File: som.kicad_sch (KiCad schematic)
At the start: 24 parts, among them U201 74LVC2G17GV

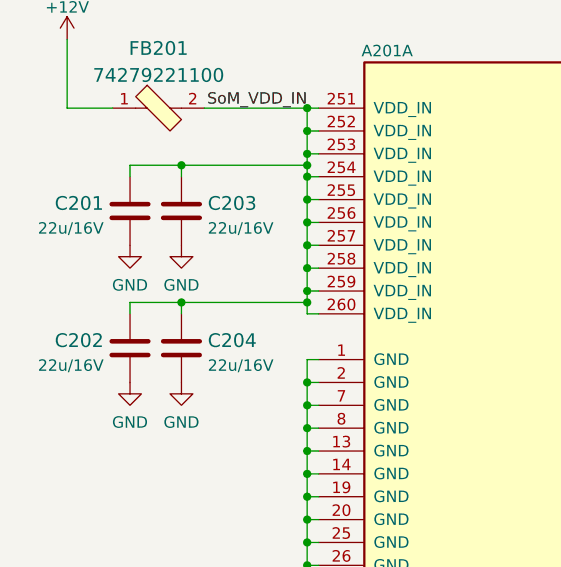
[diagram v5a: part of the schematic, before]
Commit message: Replace SoM VDD_IN caps with 25V rated ones
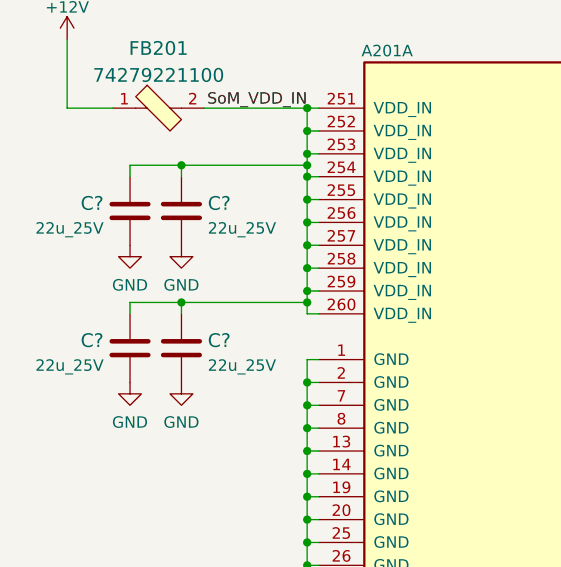
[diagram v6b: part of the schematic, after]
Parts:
- removed C201, C202, C203, C204: C_22u_0805_16V, antmicro-footprints:0805-cap, symbol antmicroCapacitorsmisc:C_22u_0805_16V
- added C? (x4): C_22u_0805_25V, antmicro-footprints:0805-cap, symbol antmicroCapacitorsmisc:C_22u_0805_25V
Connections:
- net GND: now also C?.2, C?.2, C?.2, C?.2
- net SoM_VDD_IN: now also C?.1, C?.1, C?.1, C?.1
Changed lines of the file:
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@@
-    (pin "2")
-  )
-  (symbol (lib_id "antmicroCapacitorsmisc:C_22u_0805_16V") (at 30.48 97.79 0) (unit 1)
-    (in_bom yes) (on_board yes) (fields_autoplaced)
-    (property "Reference" "C203" (id 0) (at 33.401 96.9554 0)
-      (effects (font (size 1.524 1.524)) (justify left))
-    )
-    (property "Value" "C_22u_0805_16V" (id 1) (at 30.48 101.6 0)
-      (effects (font (size 1.524 1.524)) hide)
-    )
-    (property "Footprint" "antmicro-footprints:0805-cap" (id 2) (at 35.56 92.71 0)
-      (effects (font (size 1.524 1.524)) (justify left) hide)
-    )
-    (property "Datasheet" "" (id 3) (at 30.48 97.79 0)
-      (effects (font (size 1.27 1.27)) hide)
-    )
-    (property "Manufacturer" "Murata" (id 4) (at 35.56 87.63 0)
-      (effects (font (size 1.524 1.524)) (justify left) hide)
-    )
-    (property "MPN" "GRT21BR61C226ME13L" (id 5) (at 35.56 90.17 0)
-      (effects (font (size 1.524 1.524)) (justify left) hide)
-    )
-    (property "Val" "22u/16V" (id 6) (at 33.401 99.7205 0)
-      (effects (font (size 1.27 1.27)) (justify left))
-    )
-    (pin "1")
     (pin "2")
   )
@@
     (pin "1")
   )
-  (symbol (lib_id "antmicroCapacitorsmisc:C_22u_0805_16V") (at 24.765 113.03 0) (unit 1)
-    (in_bom yes) (on_board yes) (fields_autoplaced)
-    (property "Reference" "C202" (id 0) (at 21.844 112.1954 0)
-      (effects (font (size 1.524 1.524)) (justify right))
-    )
-    (property "Value" "C_22u_0805_16V" (id 1) (at 24.765 116.84 0)
-      (effects (font (size 1.524 1.524)) hide)
-    )
-    (property "Footprint" "antmicro-footprints:0805-cap" (id 2) (at 29.845 107.95 0)
-      (effects (font (size 1.524 1.524)) (justify left) hide)
-    )
-    (property "Datasheet" "" (id 3) (at 24.765 113.03 0)
-      (effects (font (size 1.27 1.27)) hide)
-    )
-    (property "Manufacturer" "Murata" (id 4) (at 29.845 102.87 0)
-      (effects (font (size 1.524 1.524)) (justify left) hide)
-    )
-    (property "MPN" "GRT21BR61C226ME13L" (id 5) (at 29.845 105.41 0)
-      (effects (font (size 1.524 1.524)) (justify left) hide)
-    )
-    (property "Val" "22u/16V" (id 6) (at 21.844 114.9605 0)
-      (effects (font (size 1.27 1.27)) (justify right))
-    )
-    (pin "1")
-    (pin "2")
-  )
   (symbol (lib_id "antmicroResistors0402:R_0R_0402") (at 196.85 35.56 0) (unit 1)
     (in_bom yes) (on_board yes)
@@
     (pin "2")
   )
-  (symbol (lib_id "antmicroCapacitorsmisc:C_22u_0805_16V") (at 30.48 113.03 0) (unit 1)
-    (in_bom yes) (on_board yes) (fields_autoplaced)
-    (property "Reference" "C204" (id 0) (at 33.401 112.1954 0)
-      (effects (font (size 1.524 1.524)) (justify left))
-    )
-    (property "Value" "C_22u_0805_16V" (id 1) (at 30.48 116.84 0)
-      (effects (font (size 1.524 1.524)) hide)
-    )
-    (property "Footprint" "antmicro-footprints:0805-cap" (id 2) (at 35.56 107.95 0)
-      (effects (font (size 1.524 1.524)) (justify left) hide)
-    )
-    (property "Datasheet" "" (id 3) (at 30.48 113.03 0)
-      (effects (font (size 1.27 1.27)) hide)
-    )
-    (property "Manufacturer" "Murata" (id 4) (at 35.56 102.87 0)
-      (effects (font (size 1.524 1.524)) (justify left) hide)
-    )
-    (property "MPN" "GRT21BR61C226ME13L" (id 5) (at 35.56 105.41 0)
-      (effects (font (size 1.524 1.524)) (justify left) hide)
-    )
-    (property "Val" "22u/16V" (id 6) (at 33.401 114.9605 0)
-      (effects (font (size 1.27 1.27)) (justify left))
-    )
-    (pin "1")
-    (pin "2")
-  )
-  (symbol (lib_id "antmicroCapacitorsmisc:C_22u_0805_16V") (at 24.765 97.79 0) (unit 1)
-    (in_bom yes) (on_board yes) (fields_autoplaced)
-    (property "Reference" "C201" (id 0) (at 21.844 96.9554 0)
-      (effects (font (size 1.524 1.524)) (justify right))
-    )
-    (property "Value" "C_22u_0805_16V" (id 1) (at 24.765 101.6 0)
-      (effects (font (size 1.524 1.524)) hide)
-    )
-    (property "Footprint" "antmicro-footprints:0805-cap" (id 2) (at 29.845 92.71 0)
-      (effects (font (size 1.524 1.524)) (justify left) hide)
-    )
-    (property "Datasheet" "" (id 3) (at 24.765 97.79 0)
-      (effects (font (size 1.27 1.27)) hide)
-    )
-    (property "Manufacturer" "Murata" (id 4) (at 29.845 87.63 0)
-      (effects (font (size 1.524 1.524)) (justify left) hide)
-    )
-    (property "MPN" "GRT21BR61C226ME13L" (id 5) (at 29.845 90.17 0)
-      (effects (font (size 1.524 1.524)) (justify left) hide)
-    )
-    (property "Val" "22u/16V" (id 6) (at 21.844 99.7205 0)
-      (effects (font (size 1.27 1.27)) (justify right))
-    )
-    (pin "1")
-    (pin "2")
-  )
   (symbol (lib_id "antmicroResistors0402:R_0R_0402") (at 198.12 66.04 0) (mirror x) (unit 1)
     (in_bom yes) (on_board yes)
@@
     )
     (pin "1")
+  )
+  (symbol (lib_id "antmicroCapacitorsmisc:C_22u_0805_25V") (at 30.48 97.79 0) (unit 1)
+    (in_bom yes) (on_board yes) (fields_autoplaced)
+    (property "Reference" "C?" (id 0) (at 33.401 96.9554 0)
+      (effects (font (size 1.524 1.524)) (justify left))
+    )
+    (property "Value" "C_22u_0805_25V" (id 1) (at 30.48 101.6 0)
+      (effects (font (size 1.524 1.524)) hide)
+    )
+    (property "Footprint" "antmicro-footprints:0805-cap" (id 2) (at 35.56 92.71 0)
+      (effects (font (size 1.524 1.524)) (justify left) hide)
+    )
+    (property "Datasheet" "" (id 3) (at 30.48 97.79 0)
+      (effects (font (size 1.27 1.27)) hide)
+    )
+    (property "Manufacturer" "Samsung Electro-Mechanics" (id 4) (at 35.56 87.63 0)
+      (effects (font (size 1.524 1.524)) (justify left) hide)
+    )
+    (property "MPN" "CL21A226MAYNNNE" (id 5) (at 35.56 90.17 0)
+      (effects (font (size 1.524 1.524)) (justify left) hide)
+    )
+    (property "Val" "22u_25V" (id 6) (at 33.401 99.7205 0)
+      (effects (font (size 1.27 1.27)) (justify left))
+    )
+    (pin "1")
+    (pin "2")
   )
   (symbol (lib_id "power:GND") (at 97.79 212.09 0) (unit 1)
@@
     (pin "228")
   )
+  (symbol (lib_id "antmicroCapacitorsmisc:C_22u_0805_25V") (at 24.765 97.79 0) (unit 1)
+    (in_bom yes) (on_board yes) (fields_autoplaced)
+    (property "Reference" "C?" (id 0) (at 21.8441 96.9554 0)
+      (effects (font (size 1.524 1.524)) (justify right))
+    )
+    (property "Value" "C_22u_0805_25V" (id 1) (at 24.765 101.6 0)
+      (effects (font (size 1.524 1.524)) hide)
+    )
+    (property "Footprint" "antmicro-footprints:0805-cap" (id 2) (at 29.845 92.71 0)
+      (effects (font (size 1.524 1.524)) (justify left) hide)
+    )
+    (property "Datasheet" "" (id 3) (at 24.765 97.79 0)
+      (effects (font (size 1.27 1.27)) hide)
+    )
+    (property "Manufacturer" "Samsung Electro-Mechanics" (id 4) (at 29.845 87.63 0)
+      (effects (font (size 1.524 1.524)) (justify left) hide)
+    )
+    (property "MPN" "CL21A226MAYNNNE" (id 5) (at 29.845 90.17 0)
+      (effects (font (size 1.524 1.524)) (justify left) hide)
+    )
+    (property "Val" "22u_25V" (id 6) (at 21.8441 99.7205 0)
+      (effects (font (size 1.27 1.27)) (justify right))
+    )
+    (pin "1")
+    (pin "2")
+  )
   (symbol (lib_id "antmicroTestPoints:TP_SMD_0_75MM") (at 116.84 99.06 90) (unit 1)
     (in_bom yes) (on_board yes) (fields_autoplaced)
@@
     )
     (pin "1")
+  )
+  (symbol (lib_id "antmicroCapacitorsmisc:C_22u_0805_25V") (at 30.48 113.03 0) (unit 1)
+    (in_bom yes) (on_board yes) (fields_autoplaced)
+    (property "Reference" "C?" (id 0) (at 33.401 112.1954 0)
+      (effects (font (size 1.524 1.524)) (justify left))
+    )
+    (property "Value" "C_22u_0805_25V" (id 1) (at 30.48 116.84 0)
+      (effects (font (size 1.524 1.524)) hide)
+    )
+    (property "Footprint" "antmicro-footprints:0805-cap" (id 2) (at 35.56 107.95 0)
+      (effects (font (size 1.524 1.524)) (justify left) hide)
+    )
+    (property "Datasheet" "" (id 3) (at 30.48 113.03 0)
+      (effects (font (size 1.27 1.27)) hide)
+    )
+    (property "Manufacturer" "Samsung Electro-Mechanics" (id 4) (at 35.56 102.87 0)
+      (effects (font (size 1.524 1.524)) (justify left) hide)
+    )
+    (property "MPN" "CL21A226MAYNNNE" (id 5) (at 35.56 105.41 0)
+      (effects (font (size 1.524 1.524)) (justify left) hide)
+    )
+    (property "Val" "22u_25V" (id 6) (at 33.401 114.9605 0)
+      (effects (font (size 1.27 1.27)) (justify left))
+    )
+    (pin "1")
+    (pin "2")
   )
   (symbol (lib_id "antmicroPushbuttonSwitches:B3U-3000PM") (at 34.29 243.84 90) (mirror x) (unit 1)
@@
     (pin "1")
   )
+  (symbol (lib_id "antmicroCapacitorsmisc:C_22u_0805_25V") (at 24.765 113.03 0) (unit 1)
+    (in_bom yes) (on_board yes) (fields_autoplaced)
+    (property "Reference" "C?" (id 0) (at 21.8441 112.1954 0)
+      (effects (font (size 1.524 1.524)) (justify right))
+    )
+    (property "Value" "C_22u_0805_25V" (id 1) (at 24.765 116.84 0)
+      (effects (font (size 1.524 1.524)) hide)
+    )
+    (property "Footprint" "antmicro-footprints:0805-cap" (id 2) (at 29.845 107.95 0)
+      (effects (font (size 1.524 1.524)) (justify left) hide)
+    )
+    (property "Datasheet" "" (id 3) (at 24.765 113.03 0)
+      (effects (font (size 1.27 1.27)) hide)
+    )
+    (property "Manufacturer" "Samsung Electro-Mechanics" (id 4) (at 29.845 102.87 0)
+      (effects (font (size 1.524 1.524)) (justify left) hide)
+    )
+    (property "MPN" "CL21A226MAYNNNE" (id 5) (at 29.845 105.41 0)
+      (effects (font (size 1.524 1.524)) (justify left) hide)
+    )
+    (property "Val" "22u_25V" (id 6) (at 21.8441 114.9605 0)
+      (effects (font (size 1.27 1.27)) (justify right))
+    )
+    (pin "1")
+    (pin "2")
+  )
   (symbol (lib_id "power:GND") (at 30.48 101.6 0) (unit 1)

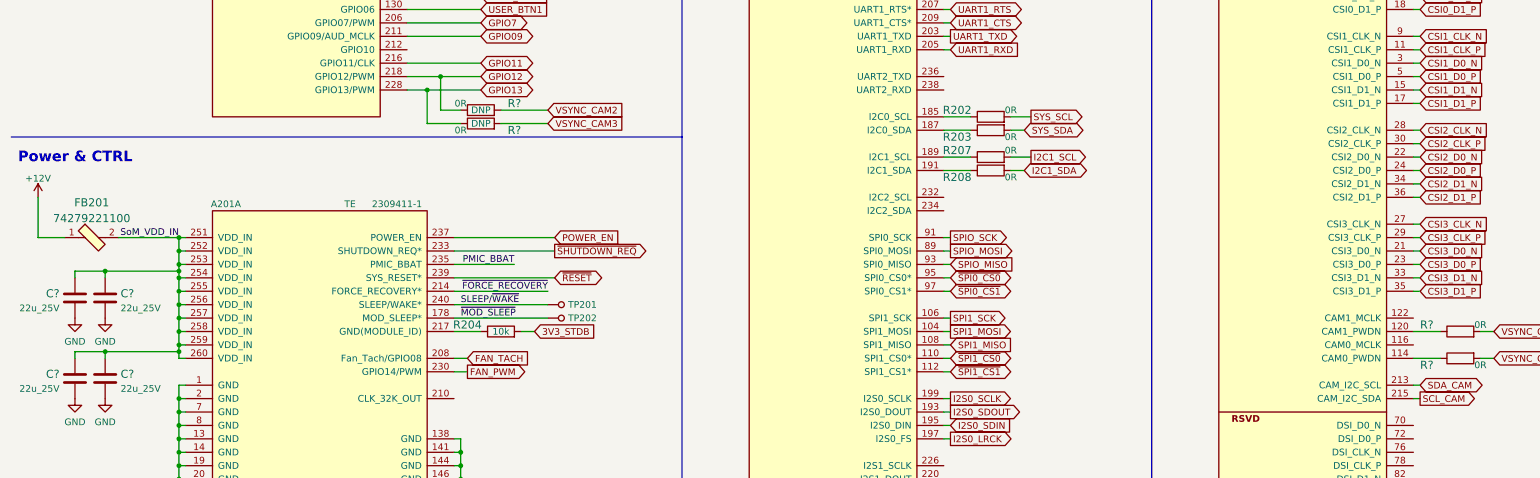
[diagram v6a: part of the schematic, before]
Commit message: Cleaned up the schematic, fixed library issues, annotated schematic
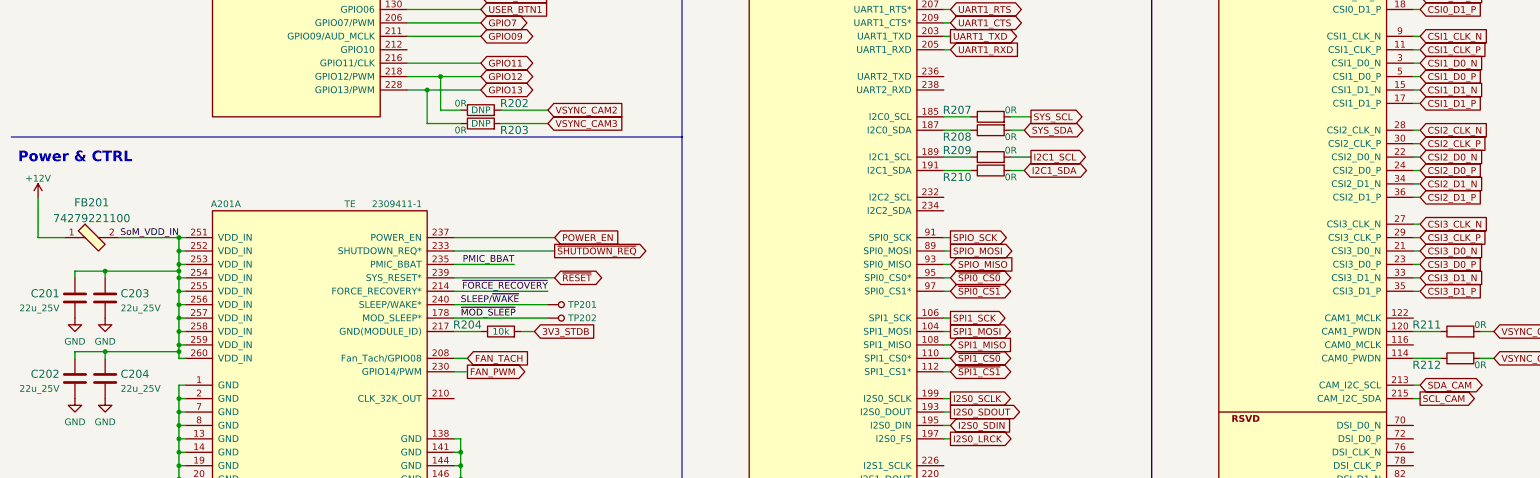
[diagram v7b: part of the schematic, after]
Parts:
- gave numbers to parts that had none: 8
- renumbered R202 to R207, R203 to R208, R207 to R209, R208 to R210
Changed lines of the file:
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@@
   (title_block
     (title "Jetson Orin NX Baseboard")
+    (date "2022-09-28")
+    (rev "0.1.0")
     (company "Antmicro Ltd")
     (comment 1 "www.antmicro.com")
@@
   (symbol (lib_id "antmicroResistors0402:R_0R_0402") (at 198.12 63.5 0) (unit 1)
     (in_bom yes) (on_board yes)
-    (property "Reference" "R202" (id 0) (at 191.77 62.23 0)
+    (property "Reference" "R207" (id 0) (at 191.77 62.23 0)
       (effects (font (size 1.524 1.524)))
     )
@@
   (symbol (lib_id "power:GND") (at 44.45 212.09 0) (unit 1)
     (in_bom yes) (on_board yes) (fields_autoplaced)
-    (property "Reference" "#PWR0206" (id 0) (at 44.45 218.44 0)
+    (property "Reference" "#PWR0207" (id 0) (at 44.45 218.44 0)
       (effects (font (size 1.27 1.27)) hide)
     )
@@
   (symbol (lib_id "antmicroResistors0402:R_0R_0402") (at 198.12 73.66 0) (mirror x) (unit 1)
     (in_bom yes) (on_board yes)
-    (property "Reference" "R208" (id 0) (at 191.77 74.93 0)
+    (property "Reference" "R210" (id 0) (at 191.77 74.93 0)
       (effects (font (size 1.524 1.524)))
     )
@@
   (symbol (lib_id "antmicroResistors0402:R_0R_0402") (at 198.12 71.12 0) (unit 1)
     (in_bom yes) (on_board yes)
-    (property "Reference" "R207" (id 0) (at 191.77 69.85 0)
+    (property "Reference" "R209" (id 0) (at 191.77 69.85 0)
       (effects (font (size 1.524 1.524)))
     )
@@
   (symbol (lib_id "power:GND") (at 64.77 250.19 0) (unit 1)
     (in_bom yes) (on_board yes) (fields_autoplaced)
-    (property "Reference" "#PWR0209" (id 0) (at 64.77 256.54 0)
+    (property "Reference" "#PWR0208" (id 0) (at 64.77 256.54 0)
       (effects (font (size 1.27 1.27)) hide)
     )
@@
   (symbol (lib_id "antmicroResistors0402:R_0R_0402") (at 101.6 64.77 0) (unit 1)
     (in_bom yes) (on_board yes)
-    (property "Reference" "R?" (id 0) (at 107.95 66.04 0)
+    (property "Reference" "R203" (id 0) (at 107.95 66.04 0)
       (effects (font (size 1.524 1.524)))
     )
@@
   (symbol (lib_id "antmicroResistors0402:R_0R_0402") (at 198.12 66.04 0) (mirror x) (unit 1)
     (in_bom yes) (on_board yes)
-    (property "Reference" "R203" (id 0) (at 191.77 67.31 0)
+    (property "Reference" "R208" (id 0) (at 191.77 67.31 0)
       (effects (font (size 1.524 1.524)))
     )
@@
   (symbol (lib_id "antmicroCapacitorsmisc:C_22u_0805_25V") (at 30.48 97.79 0) (unit 1)
     (in_bom yes) (on_board yes) (fields_autoplaced)
-    (property "Reference" "C?" (id 0) (at 33.401 96.9554 0)
+    (property "Reference" "C203" (id 0) (at 33.401 96.9554 0)
       (effects (font (size 1.524 1.524)) (justify left))
     )
@@
   (symbol (lib_id "power:GND") (at 97.79 212.09 0) (unit 1)
     (in_bom yes) (on_board yes) (fields_autoplaced)
-    (property "Reference" "#PWR0207" (id 0) (at 97.79 218.44 0)
+    (property "Reference" "#PWR0209" (id 0) (at 97.79 218.44 0)
       (effects (font (size 1.27 1.27)) hide)
     )
@@
   (symbol (lib_id "antmicroCapacitorsmisc:C_22u_0805_25V") (at 24.765 97.79 0) (unit 1)
     (in_bom yes) (on_board yes) (fields_autoplaced)
-    (property "Reference" "C?" (id 0) (at 21.8441 96.9554 0)
+    (property "Reference" "C201" (id 0) (at 21.8441 96.9554 0)
       (effects (font (size 1.524 1.524)) (justify right))
     )
@@
   (symbol (lib_id "antmicroCapacitorsmisc:C_22u_0805_25V") (at 30.48 113.03 0) (unit 1)
     (in_bom yes) (on_board yes) (fields_autoplaced)
-    (property "Reference" "C?" (id 0) (at 33.401 112.1954 0)
+    (property "Reference" "C204" (id 0) (at 33.401 112.1954 0)
       (effects (font (size 1.524 1.524)) (justify left))
     )
@@
   (symbol (lib_id "antmicroResistors0402:R_0R_0402") (at 287.02 109.22 0) (mirror x) (unit 1)
     (in_bom yes) (on_board yes)
-    (property "Reference" "R?" (id 0) (at 280.67 110.49 0)
+    (property "Reference" "R212" (id 0) (at 280.67 110.49 0)
       (effects (font (size 1.524 1.524)))
     )
@@
   (symbol (lib_id "antmicroResistors0402:R_0R_0402") (at 101.6 62.23 0) (unit 1)
     (in_bom yes) (on_board yes)
-    (property "Reference" "R?" (id 0) (at 107.95 60.96 0)
+    (property "Reference" "R202" (id 0) (at 107.95 60.96 0)
       (effects (font (size 1.524 1.524)))
     )
@@
   (symbol (lib_id "antmicroCapacitorsmisc:C_22u_0805_25V") (at 24.765 113.03 0) (unit 1)
     (in_bom yes) (on_board yes) (fields_autoplaced)
-    (property "Reference" "C?" (id 0) (at 21.8441 112.1954 0)
+    (property "Reference" "C202" (id 0) (at 21.8441 112.1954 0)
       (effects (font (size 1.524 1.524)) (justify right))
     )
@@
   (symbol (lib_id "antmicroResistors0402:R_0R_0402") (at 287.02 104.14 0) (unit 1)
     (in_bom yes) (on_board yes)
-    (property "Reference" "R?" (id 0) (at 280.67 102.87 0)
+    (property "Reference" "R211" (id 0) (at 280.67 102.87 0)
       (effects (font (size 1.524 1.524)))
     )
@@
   (symbol (lib_id "power:GND") (at 34.29 250.19 0) (unit 1)
     (in_bom yes) (on_board yes) (fields_autoplaced)
-    (property "Reference" "#PWR0208" (id 0) (at 34.29 256.54 0)
+    (property "Reference" "#PWR0206" (id 0) (at 34.29 256.54 0)
       (effects (font (size 1.27 1.27)) hide)
     )
